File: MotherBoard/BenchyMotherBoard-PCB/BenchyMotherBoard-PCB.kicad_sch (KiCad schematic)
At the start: 0 parts

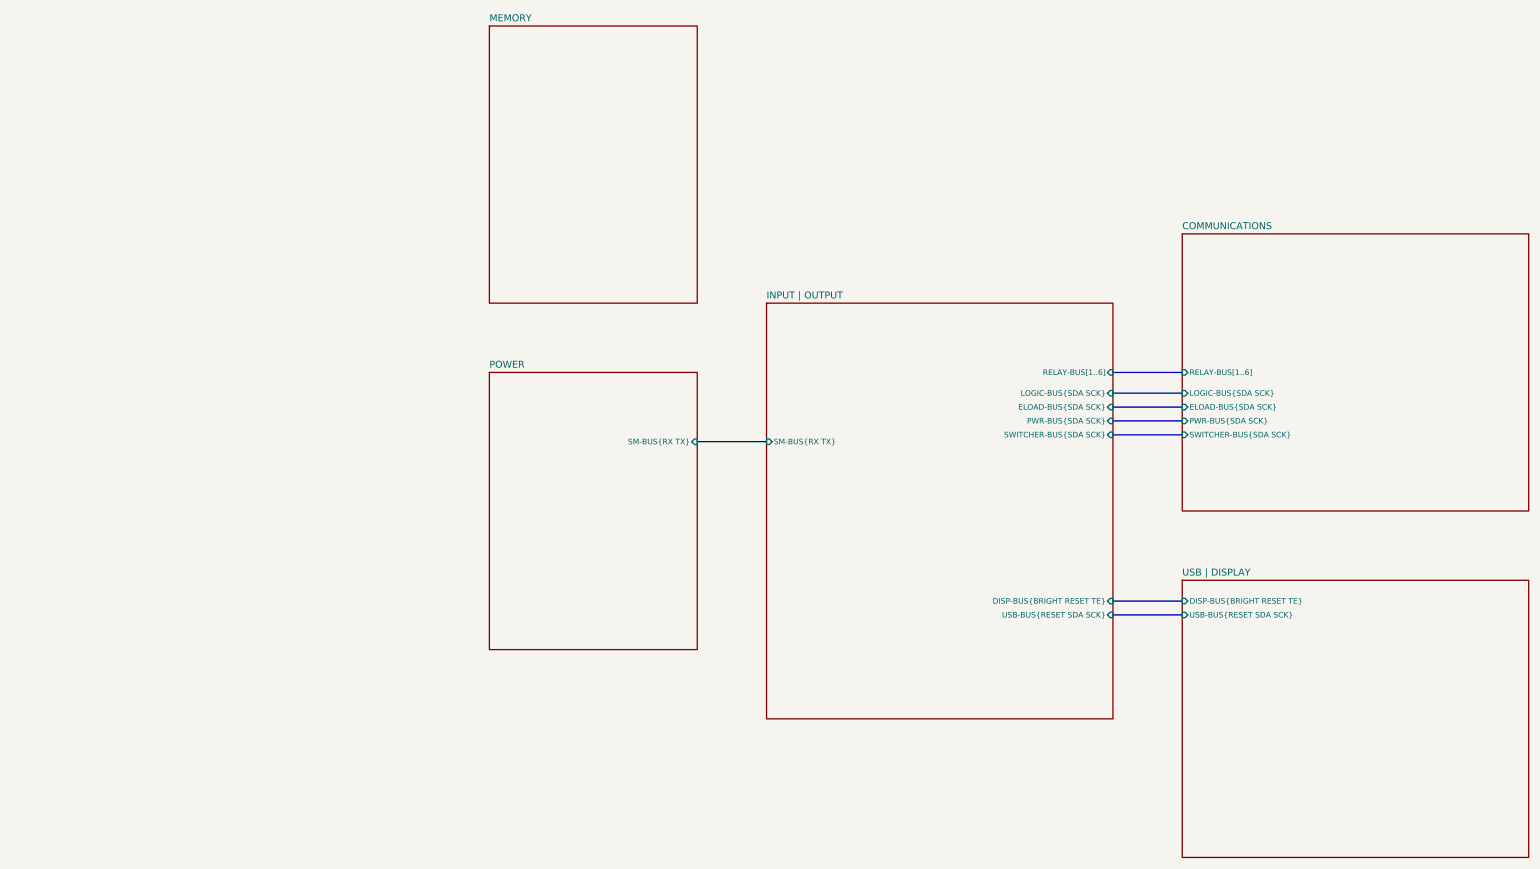
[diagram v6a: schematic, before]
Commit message: Add volt meter PCB
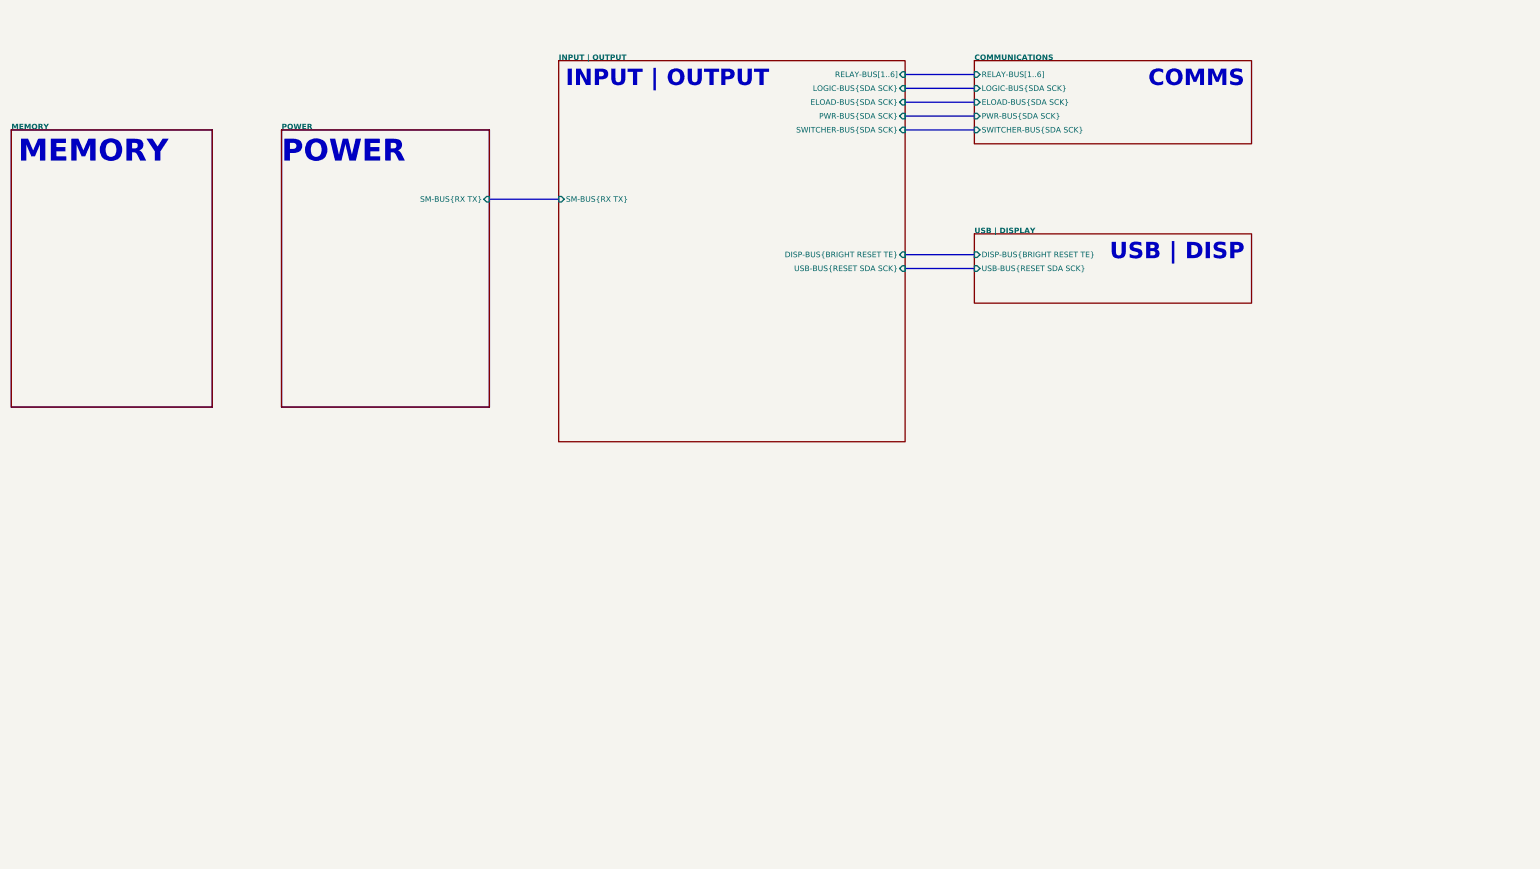
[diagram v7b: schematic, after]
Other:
- note added: "COMMS"
- note added: "INPUT | OUTPUT"
- note added: "MEMORY"
- note added: "POWER"
- note added: "USB | DISP"
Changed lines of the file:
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@@
 (kicad_sch (version 20230121) (generator eeschema)
-  (paper "A2")
+  (paper "User" 310.007 124.993)
   (title_block
     (title "Benchy Reloaded")
@@
     (company "Daxxn Industries")
   )
-  (bus (pts (xy 139.7 101.6) (xy 152.4 101.6))
+  (bus (pts (xy 177.8 67.31) (xy 190.5 67.31))
     (stroke (width 0) (type default))
   )
-  (bus (pts (xy 215.9 88.9) (xy 228.6 88.9))
+  (bus (pts (xy 177.8 41.91) (xy 190.5 41.91))
     (stroke (width 0) (type default))
   )
-  (bus (pts (xy 215.9 100.33) (xy 228.6 100.33))
+  (bus (pts (xy 177.8 34.29) (xy 190.5 34.29))
     (stroke (width 0) (type default))
   )
-  (bus (pts (xy 215.9 130.81) (xy 228.6 130.81))
+  (bus (pts (xy 101.6 57.15) (xy 114.3 57.15))
     (stroke (width 0) (type default))
   )
-  (bus (pts (xy 215.9 92.71) (xy 228.6 92.71))
+  (bus (pts (xy 177.8 44.45) (xy 190.5 44.45))
     (stroke (width 0) (type default))
   )
-  (bus (pts (xy 215.9 95.25) (xy 228.6 95.25))
+  (bus (pts (xy 177.8 36.83) (xy 190.5 36.83))
     (stroke (width 0) (type default))
   )
-  (bus (pts (xy 215.9 97.79) (xy 228.6 97.79))
+  (bus (pts (xy 177.8 39.37) (xy 190.5 39.37))
     (stroke (width 0) (type default))
   )
-  (bus (pts (xy 215.9 133.35) (xy 228.6 133.35))
+  (bus (pts (xy 177.8 69.85) (xy 190.5 69.85))
     (stroke (width 0) (type default))
   )
-  (sheet (at 101.6 25.4) (size 38.1 50.8) (fields_autoplaced)
+  (text_box ""
+    (at 63.5 44.45 0) (size 38.1 50.8)
+    (stroke (width 0) (type default))
+    (fill (type none))
+    (effects (font (size 1.016 1.016) bold) (justify left top) (href "#2"))
+  )
+  (text_box ""
+    (at 13.97 44.45 0) (size 36.83 50.8)
+    (stroke (width 0) (type default))
+    (fill (type none))
+    (effects (font (size 1.016 1.016) bold) (justify left top) (href "#3"))
+  )
+  (text "USB | DISP" (at 240.03 68.58 0)
+    (effects (font (size 3 3) bold) (justify right bottom) (href "#5"))
+  )
+  (text "COMMS" (at 240.03 36.83 0)
+    (effects (font (size 3 3) bold) (justify right bottom) (href "#7"))
+  )
+  (text "POWER" (at 63.5 50.8 0)
+    (effects (font (size 4 4) bold) (justify left bottom) (href "#2"))
+  )
+  (text "MEMORY" (at 15.24 50.8 0)
+    (effects (font (size 4 4) bold) (justify left bottom) (href "#3"))
+  )
+  (text "INPUT | OUTPUT" (at 115.57 36.83 0)
+    (effects (font (size 3 3) bold) (justify left bottom) (href "#4"))
+  )
+  (sheet (at 13.97 44.45) (size 36.83 50.8)
     (stroke (width 0.1524) (type solid))
     (fill (color 0 0 0 0.0000))
-    (property "Sheetname" "MEMORY" (at 101.6 24.6884 0)
-      (effects (font (size 1.27 1.27)) (justify left bottom))
+    (property "Sheetname" "MEMORY" (at 13.97 44.45 0)
+      (effects (font (size 1 1) bold) (justify left bottom))
     )
-    (property "Sheetfile" "memory.kicad_sch" (at 101.6 76.7846 0)
+    (property "Sheetfile" "memory.kicad_sch" (at 13.97 95.8346 0)
       (effects (font (size 1.27 1.27)) (justify left top) hide)
     )
@@
     )
   )
-  (sheet (at 228.6 127) (size 63.5 50.8) (fields_autoplaced)
+  (sheet (at 190.5 63.5) (size 50.8 12.7)
     (stroke (width 0.1524) (type solid))
     (fill (color 0 0 0 0.0000))
-    (property "Sheetname" "USB | DISPLAY" (at 228.6 126.2884 0)
-      (effects (font (size 1.27 1.27)) (justify left bottom))
+    (property "Sheetname" "USB | DISPLAY" (at 190.5 63.5 0)
+      (effects (font (size 1 1) bold) (justify left bottom))
     )
-    (property "Sheetfile" "usb.kicad_sch" (at 228.6 178.3846 0)
+    (property "Sheetfile" "usb.kicad_sch" (at 190.5 114.8846 0)
       (effects (font (size 1.27 1.27)) (justify left top) hide)
     )
-    (pin "DISP-BUS{BRIGHT RESET TE}" input (at 228.6 130.81 180)
+    (pin "DISP-BUS{BRIGHT RESET TE}" input (at 190.5 67.31 180)
       (effects (font (size 1.016 1.016)) (justify left))
     )
-    (pin "USB-BUS{RESET SDA SCK}" input (at 228.6 133.35 180)
+    (pin "USB-BUS{RESET SDA SCK}" input (at 190.5 69.85 180)
       (effects (font (size 1.016 1.016)) (justify left))
     )
@@
     )
   )
-  (sheet (at 152.4 76.2) (size 63.5 76.2) (fields_autoplaced)
+  (sheet (at 114.3 31.75) (size 63.5 69.85)
     (stroke (width 0.1524) (type solid))
     (fill (color 0 0 0 0.0000))
-    (property "Sheetname" "INPUT | OUTPUT" (at 152.4 75.4884 0)
-      (effects (font (size 1.27 1.27)) (justify left bottom))
+    (property "Sheetname" "INPUT | OUTPUT" (at 114.3 31.75 0)
+      (effects (font (size 1 1) bold) (justify left bottom))
     )
-    (property "Sheetfile" "gpio.kicad_sch" (at 152.4 152.9846 0)
+    (property "Sheetfile" "gpio.kicad_sch" (at 114.3 108.5346 0)
       (effects (font (size 1.27 1.27)) (justify left top) hide)
     )
-    (pin "SM-BUS{RX TX}" input (at 152.4 101.6 180)
+    (pin "SM-BUS{RX TX}" input (at 114.3 57.15 180)
       (effects (font (size 1.016 1.016)) (justify left))
     )
-    (pin "USB-BUS{RESET SDA SCK}" input (at 215.9 133.35 0)
+    (pin "USB-BUS{RESET SDA SCK}" input (at 177.8 69.85 0)
       (effects (font (size 1.016 1.016)) (justify right))
     )
-    (pin "LOGIC-BUS{SDA SCK}" input (at 215.9 92.71 0)
+    (pin "LOGIC-BUS{SDA SCK}" input (at 177.8 36.83 0)
       (effects (font (size 1.016 1.016)) (justify right))
     )
-    (pin "DISP-BUS{BRIGHT RESET TE}" input (at 215.9 130.81 0)
+    (pin "DISP-BUS{BRIGHT RESET TE}" input (at 177.8 67.31 0)
       (effects (font (size 1.016 1.016)) (justify right))
     )
-    (pin "ELOAD-BUS{SDA SCK}" input (at 215.9 95.25 0)
+    (pin "ELOAD-BUS{SDA SCK}" input (at 177.8 39.37 0)
       (effects (font (size 1.016 1.016)) (justify right))
     )
-    (pin "RELAY-BUS[1..6]" input (at 215.9 88.9 0)
+    (pin "RELAY-BUS[1..6]" input (at 177.8 34.29 0)
       (effects (font (size 1.016 1.016)) (justify right))
     )
-    (pin "PWR-BUS{SDA SCK}" input (at 215.9 97.79 0)
+    (pin "PWR-BUS{SDA SCK}" input (at 177.8 41.91 0)
       (effects (font (size 1.016 1.016)) (justify right))
     )
-    (pin "SWITCHER-BUS{SDA SCK}" input (at 215.9 100.33 0)
+    (pin "SWITCHER-BUS{SDA SCK}" input (at 177.8 44.45 0)
       (effects (font (size 1.016 1.016)) (justify right))
     )
@@
     )
   )
-  (sheet (at 101.6 88.9) (size 38.1 50.8) (fields_autoplaced)
+  (sheet (at 63.5 44.45) (size 38.1 50.8)
     (stroke (width 0.1524) (type solid))
     (fill (color 0 0 0 0.0000))
-    (property "Sheetname" "POWER" (at 101.6 88.1884 0)
-      (effects (font (size 1.27 1.27)) (justify left bottom))
+    (property "Sheetname" "POWER" (at 63.5 44.45 0)
+      (effects (font (size 1 1) bold) (justify left bottom))
     )
-    (property "Sheetfile" "power.kicad_sch" (at 101.6 140.2846 0)
+    (property "Sheetfile" "power.kicad_sch" (at 63.5 95.8346 0)
       (effects (font (size 1.27 1.27)) (justify left top) hide)
     )
-    (pin "SM-BUS{RX TX}" input (at 139.7 101.6 0)
+    (property "link" "#2" (at 63.5 44.45 0)
+      (effects (font (size 1.27 1.27)) hide)
+    )
+    (pin "SM-BUS{RX TX}" input (at 101.6 57.15 0)
       (effects (font (size 1.016 1.016)) (justify right))
     )
@@
     )
   )
-  (sheet (at 228.6 63.5) (size 63.5 50.8) (fields_autoplaced)
+  (sheet (at 190.5 31.75) (size 50.8 15.24)
     (stroke (width 0.1524) (type solid))
     (fill (color 0 0 0 0.0000))
-    (property "Sheetname" "COMMUNICATIONS" (at 228.6 62.7884 0)
-      (effects (font (size 1.27 1.27)) (justify left bottom))
+    (property "Sheetname" "COMMUNICATIONS" (at 190.5 31.75 0)
+      (effects (font (size 1 1) bold) (justify left bottom))
     )
-    (property "Sheetfile" "comms.kicad_sch" (at 228.6 114.8846 0)
+    (property "Sheetfile" "comms.kicad_sch" (at 190.5 83.1346 0)
       (effects (font (size 1.27 1.27)) (justify left top) hide)
     )
-    (pin "RELAY-BUS[1..6]" input (at 228.6 88.9 180)
+    (pin "RELAY-BUS[1..6]" input (at 190.5 34.29 180)
       (effects (font (size 1.016 1.016)) (justify left))
     )
-    (pin "LOGIC-BUS{SDA SCK}" input (at 228.6 92.71 180)
+    (pin "LOGIC-BUS{SDA SCK}" input (at 190.5 36.83 180)
       (effects (font (size 1.016 1.016)) (justify left))
     )
-    (pin "ELOAD-BUS{SDA SCK}" input (at 228.6 95.25 180)
+    (pin "ELOAD-BUS{SDA SCK}" input (at 190.5 39.37 180)
       (effects (font (size 1.016 1.016)) (justify left))
     )
-    (pin "PWR-BUS{SDA SCK}" input (at 228.6 97.79 180)
+    (pin "PWR-BUS{SDA SCK}" input (at 190.5 41.91 180)
       (effects (font (size 1.016 1.016)) (justify left))
     )
-    (pin "SWITCHER-BUS{SDA SCK}" input (at 228.6 100.33 180)
+    (pin "SWITCHER-BUS{SDA SCK}" input (at 190.5 44.45 180)
       (effects (font (size 1.016 1.016)) (justify left))
     )
